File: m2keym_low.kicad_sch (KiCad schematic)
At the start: 14 parts, among them J5 Bus_M.2_MDT180M03001

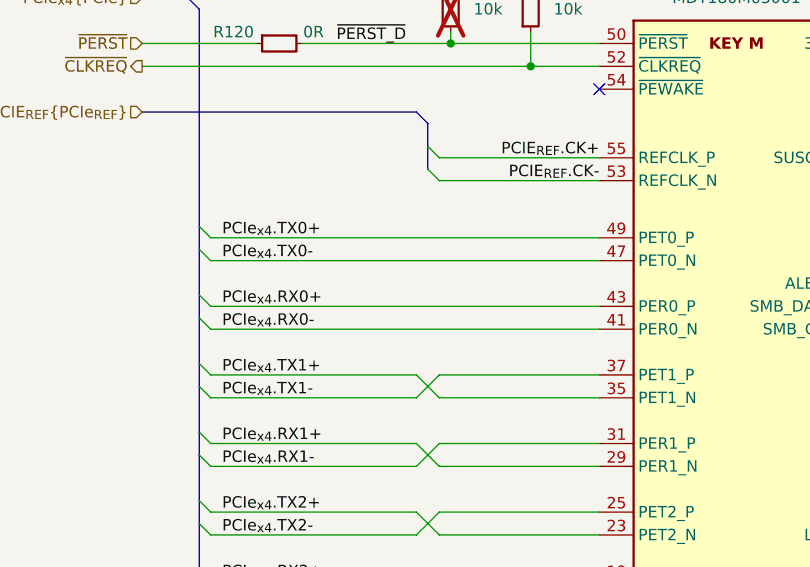
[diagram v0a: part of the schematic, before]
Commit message: [#70030] Routed PCIe
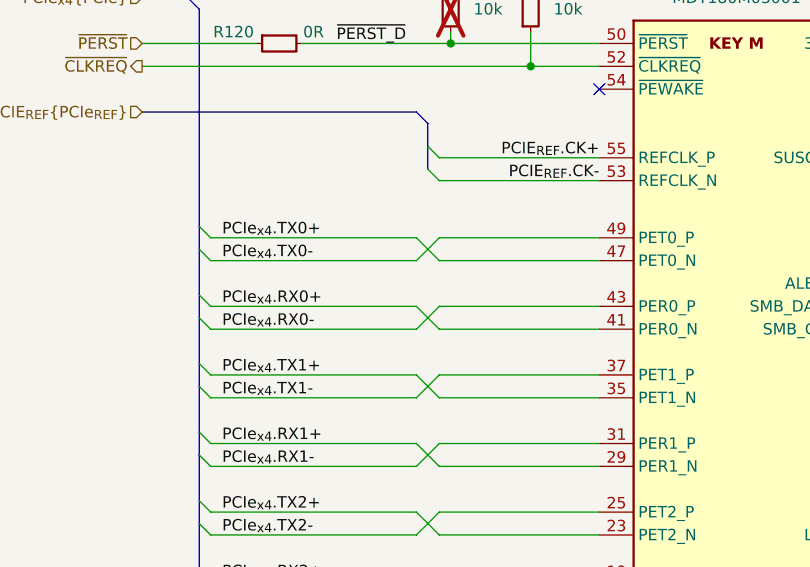
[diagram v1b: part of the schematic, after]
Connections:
- net PCIe_{x4}.RX0+: now also J5.41 (PER0_N); no longer J5.43 (PER0_P)
- net PCIe_{x4}.RX0-: now also J5.43 (PER0_P); no longer J5.41 (PER0_N)
- net PCIe_{x4}.TX0+: now also J5.47 (PET0_N); no longer J5.49 (PET0_P)
- net PCIe_{x4}.TX0-: now also J5.49 (PET0_P); no longer J5.47 (PET0_N)
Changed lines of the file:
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@@
 	(wire
 		(pts
-			(xy 200.66 118.11) (xy 157.48 118.11)
+			(xy 200.66 118.11) (xy 182.88 118.11)
+		)
+		(stroke
+			(width 0)
+			(type default)
+		)
+	)
+	(wire
+		(pts
+			(xy 182.88 110.49) (xy 200.66 110.49)
 		)
 		(stroke
@@
 	(wire
 		(pts
-			(xy 200.66 120.65) (xy 157.48 120.65)
+			(xy 200.66 120.65) (xy 182.88 120.65)
 		)
 		(stroke
@@
 	(wire
 		(pts
-			(xy 157.48 113.03) (xy 200.66 113.03)
+			(xy 157.48 113.03) (xy 180.34 113.03)
 		)
 		(stroke
@@
 	(wire
 		(pts
+			(xy 180.34 118.11) (xy 182.88 120.65)
+		)
+		(stroke
+			(width 0)
+			(type default)
+		)
+	)
+	(wire
+		(pts
 			(xy 267.97 85.09) (xy 257.81 85.09)
 		)
@@
 	(wire
 		(pts
-			(xy 157.48 110.49) (xy 200.66 110.49)
+			(xy 157.48 110.49) (xy 180.34 110.49)
 		)
 		(stroke
@@
 	(wire
 		(pts
+			(xy 182.88 113.03) (xy 200.66 113.03)
+		)
+		(stroke
+			(width 0)
+			(type default)
+		)
+	)
+	(wire
+		(pts
 			(xy 157.48 140.97) (xy 180.34 140.97)
 		)
@@
 	(wire
 		(pts
+			(xy 180.34 110.49) (xy 182.88 113.03)
+		)
+		(stroke
+			(width 0)
+			(type default)
+		)
+	)
+	(wire
+		(pts
 			(xy 180.34 140.97) (xy 182.88 143.51)
 		)
@@
 	(wire
 		(pts
+			(xy 182.88 118.11) (xy 180.34 120.65)
+		)
+		(stroke
+			(width 0)
+			(type default)
+		)
+	)
+	(wire
+		(pts
 			(xy 182.88 135.89) (xy 200.66 135.89)
 		)
@@
 	(wire
 		(pts
+			(xy 180.34 120.65) (xy 157.48 120.65)
+		)
+		(stroke
+			(width 0)
+			(type default)
+		)
+	)
+	(wire
+		(pts
 			(xy 193.04 87.63) (xy 193.04 91.44)
 		)
@@
 	(wire
 		(pts
+			(xy 182.88 110.49) (xy 180.34 113.03)
+		)
+		(stroke
+			(width 0)
+			(type default)
+		)
+	)
+	(wire
+		(pts
 			(xy 232.41 85.09) (xy 237.49 85.09)
 		)
@@
 		)
 		(stroke
+			(width 0)
+			(type default)
+		)
+	)
+	(wire
+		(pts
+			(xy 180.34 118.11) (xy 157.48 118.11)
+		)
+		(stroke
